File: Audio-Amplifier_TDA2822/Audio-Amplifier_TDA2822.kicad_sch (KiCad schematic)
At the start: 33 parts, among them J1 Conn_SPKR_L, J2 Conn_SPKR_L, U1 TDA2822M_2, U2 NE5532

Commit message: class D amp
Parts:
- C11, C12, C13, C7, C8, C9: footprint (none) -> Capacitor_THT:CP_Radial_D5.0mm_P2.50mm
- U1: footprint (none) -> Package_DIP:DIP-8_W7.62mm_LongPads
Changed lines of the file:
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@@
 			)
 		)
-		(property "Footprint" ""
+		(property "Footprint" "Package_DIP:DIP-8_W7.62mm_LongPads"
 			(at 167.64 43.18 0)
 			(effects
@@
 			)
 		)
-		(property "Footprint" ""
+		(property "Footprint" "Capacitor_THT:CP_Radial_D5.0mm_P2.50mm"
 			(at 172.72 59.3852 0)
 			(effects
@@
 			)
 		)
-		(property "Footprint" ""
+		(property "Footprint" "Capacitor_THT:CP_Radial_D5.0mm_P2.50mm"
 			(at 175.26 120.3452 0)
 			(effects
@@
 			)
 		)
-		(property "Footprint" ""
+		(property "Footprint" "Capacitor_THT:CP_Radial_D5.0mm_P2.50mm"
 			(at 31.4452 83.82 0)
 			(effects
@@
 			)
 		)
-		(property "Footprint" ""
+		(property "Footprint" "Capacitor_THT:CP_Radial_D5.0mm_P2.50mm"
 			(at 129.2352 165.1 0)
 			(effects
@@
 			)
 		)
-		(property "Footprint" ""
+		(property "Footprint" "Package_DIP:DIP-8_W7.62mm_LongPads"
 			(at 60.96 92.71 0)
 			(effects
@@
 			)
 		)
-		(property "Footprint" ""
+		(property "Footprint" "Capacitor_THT:CP_Radial_D5.0mm_P2.50mm"
 			(at 190.1952 62.23 0)
 			(effects
@@
 			)
 		)
-		(property "Footprint" ""
+		(property "Footprint" "Capacitor_THT:CP_Radial_D5.0mm_P2.50mm"
 			(at 186.69 103.1748 0)
 			(effects
@@
 			)
 		)
-		(property "Footprint" ""
+		(property "Footprint" "Package_DIP:DIP-8_W7.62mm_LongPads"
 			(at 167.64 104.14 0)
 			(effects

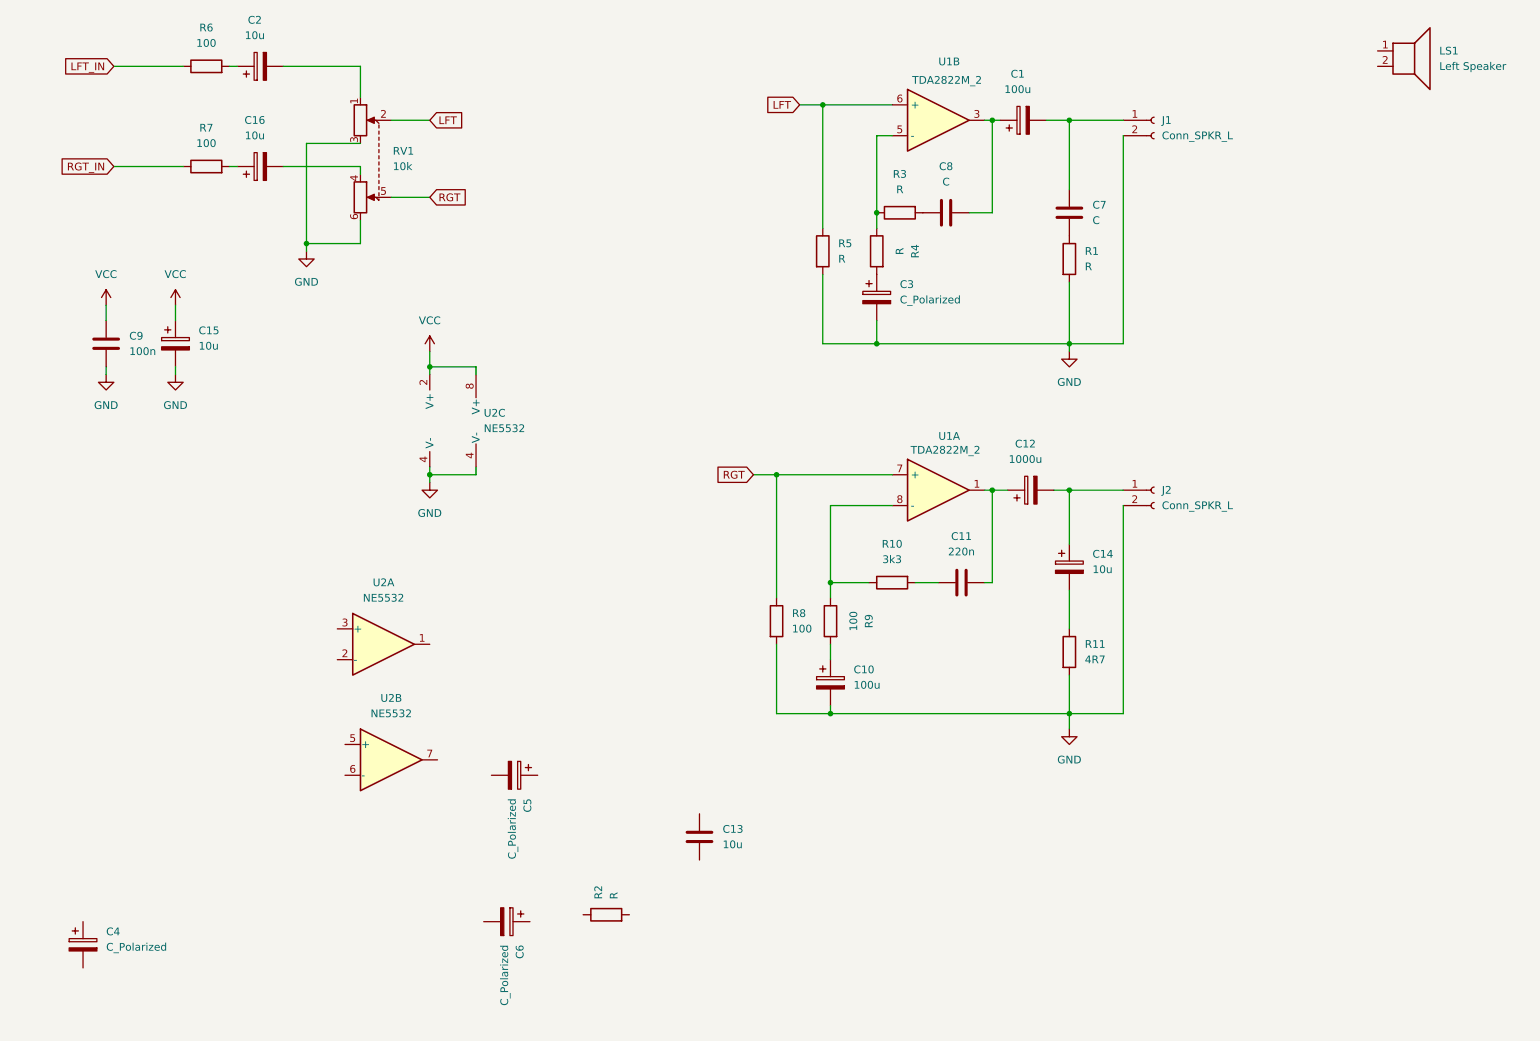
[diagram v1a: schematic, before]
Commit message: class D amp
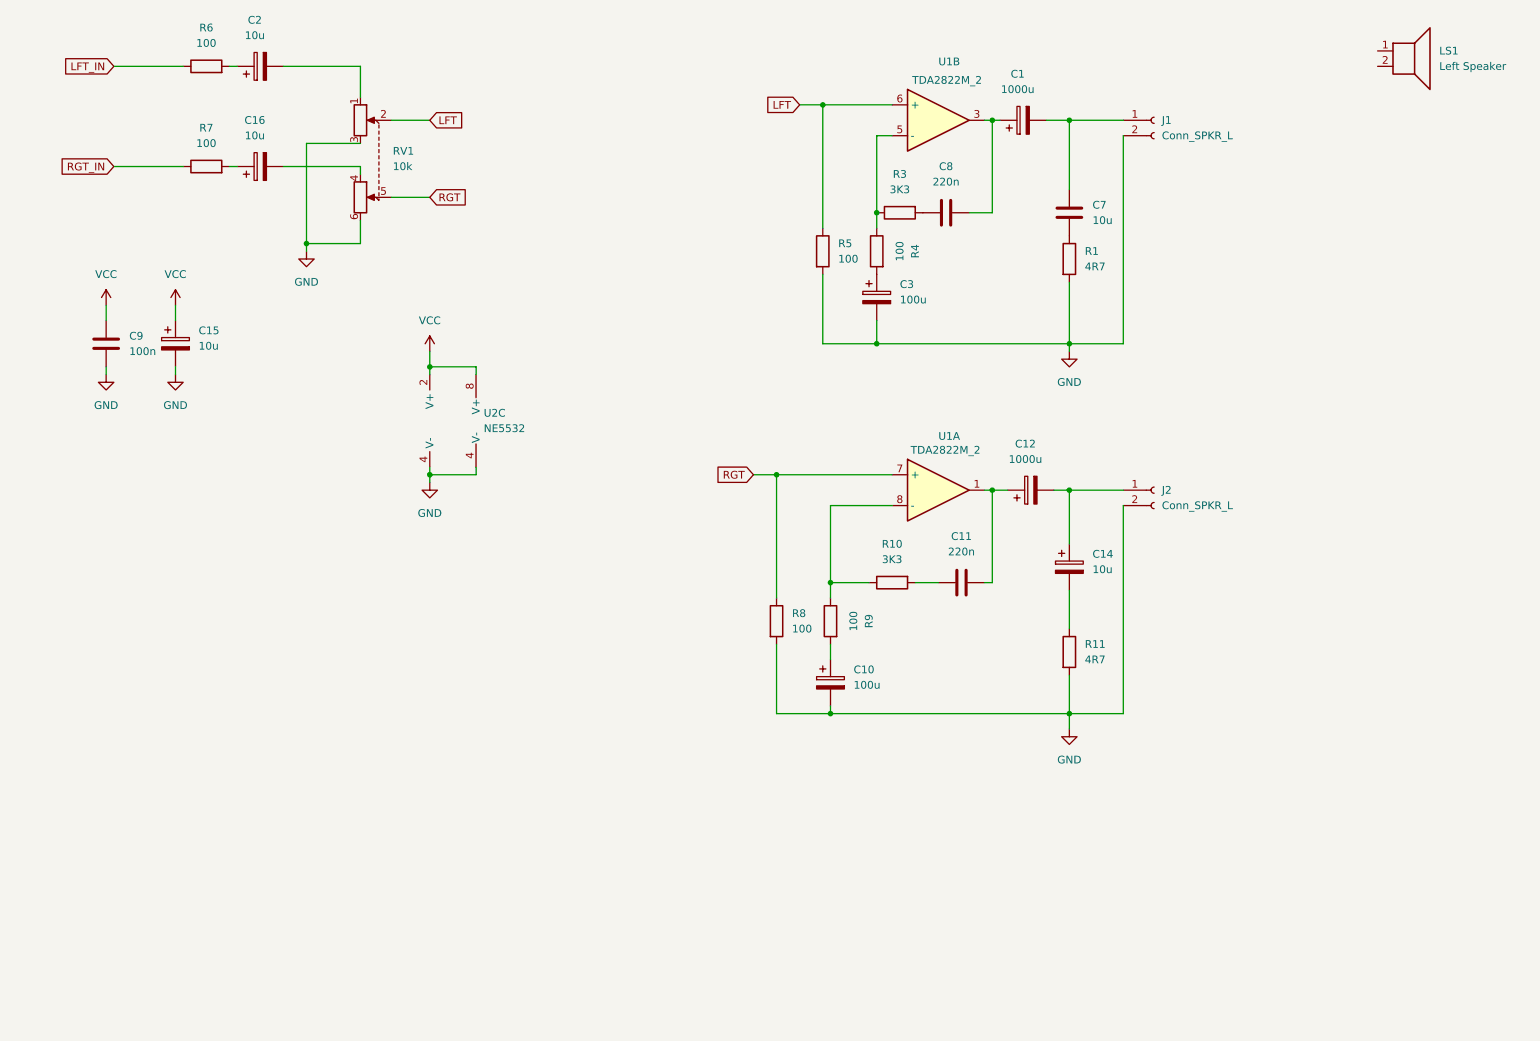
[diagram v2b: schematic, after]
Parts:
- removed C13: 10u, Capacitor_THT:CP_Radial_D5.0mm_P2.50mm, symbol Device:C
- removed C4, C5, C6: C_Polarized, Capacitor_THT:CP_Radial_D5.0mm_P2.50mm, symbol Device:C_Polarized
- removed R2: R, Resistor_THT:R_Axial_DIN0204_L3.6mm_D1.6mm_P5.08mm_Vertical, symbol Device:R
- removed unit 1 of U2
- removed unit 2 of U2
- C1: value 100u -> 1000u
- C3: value C_Polarized -> 100u
- C7: value C -> 10u
- C8: value C -> 220n
- R1: value R -> 4R7
- R10: value 3k3 -> 3K3
- R3: value R -> 3K3
- R4, R5: value R -> 100
- RV1: footprint Potentiometer_SMD:Potentiometer_Bourns_3224G_Horizontal -> Potentiometer_THT:Potentiometer_Bourns_PTV112-4_Dual_Vertical

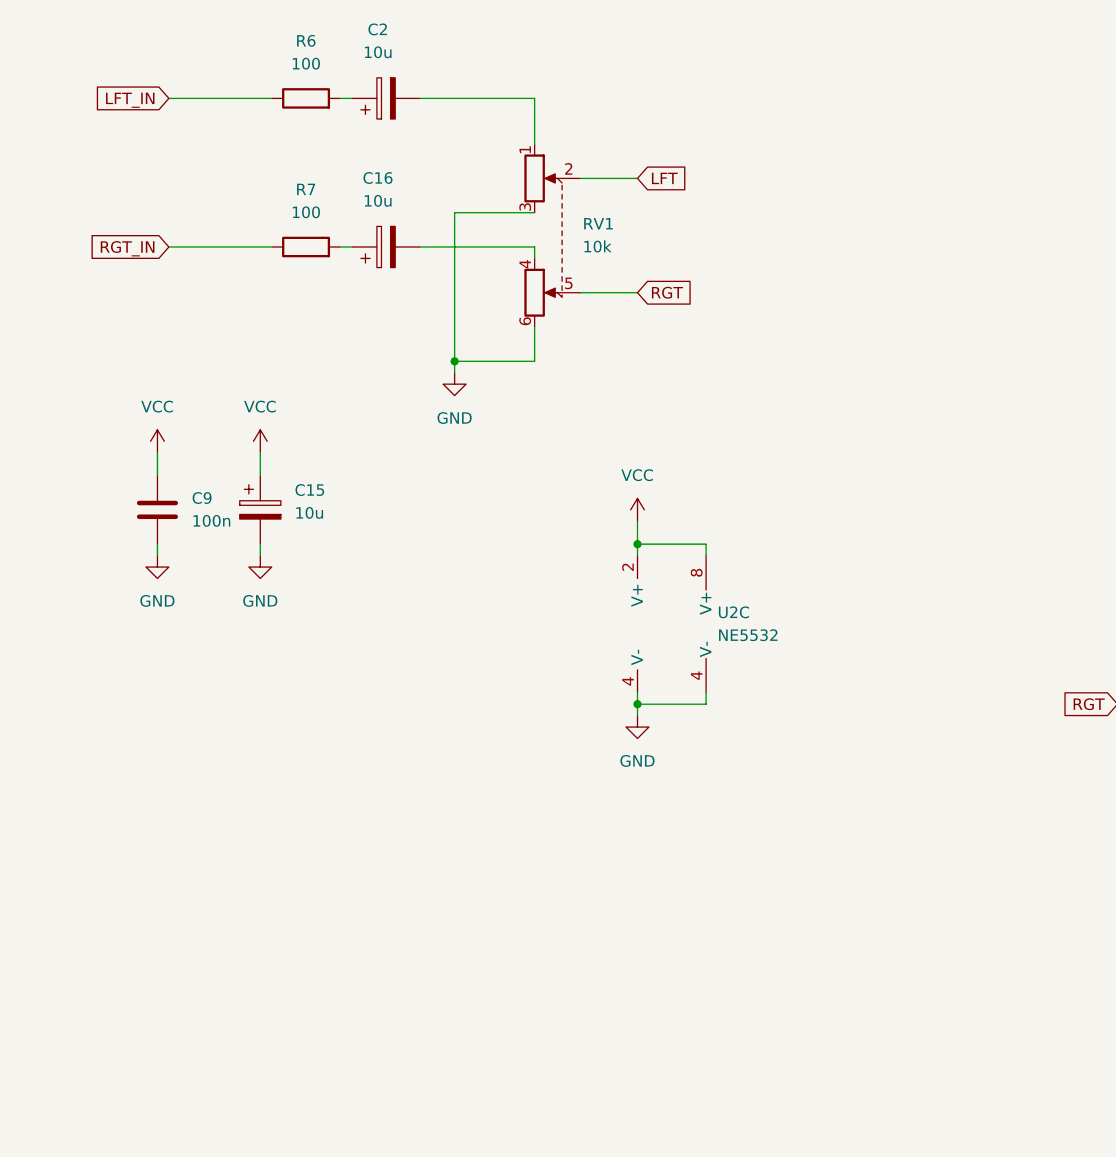
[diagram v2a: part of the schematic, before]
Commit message: class D amp
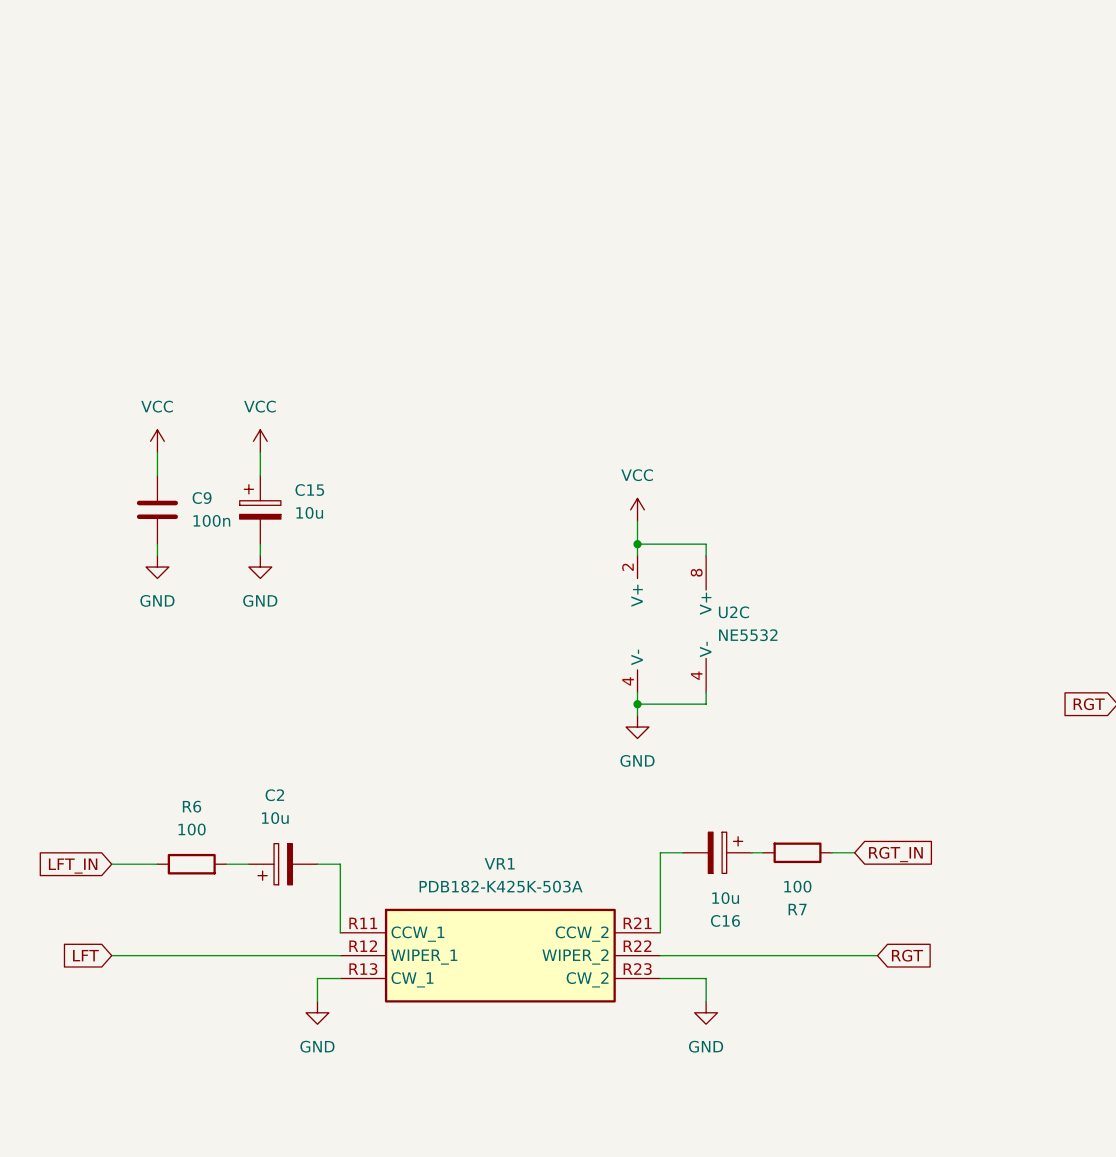
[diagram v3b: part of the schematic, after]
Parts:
- removed RV1: 10k, Potentiometer_THT:Potentiometer_Bourns_PTV112-4_Dual_Vertical, symbol Device:R_Potentiometer_Dual
- added VR1: PDB182-K425K-503A, PDB182K425K503A, symbol project:PDB182-K425K-503A
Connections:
- net GND: now also VR1.R13 (CW_1), VR1.R23 (CW_2)
- net LFT: now also VR1.R12 (WIPER_1)
- net RGT: now also VR1.R22 (WIPER_2)
- net at C16.2: now also VR1.R21 (CCW_2)
- net at C2.2: now also VR1.R11 (CCW_1)
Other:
- moved on the sheet: C16, C2, R6, R7

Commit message: class D amp
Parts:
- C1, U2: footprint (none) -> Capacitor_THT:CP_Radial_D8.0mm_P5.00mm
- C12: footprint Capacitor_THT:CP_Radial_D5.0mm_P2.50mm -> Capacitor_THT:CP_Radial_D8.0mm_P5.00mm
- VR1: footprint PDB182K425K503A -> project:PDB182K425K503A
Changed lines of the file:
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@@
 			)
 		)
-		(property "Footprint" ""
+		(property "Footprint" "Capacitor_THT:CP_Radial_D8.0mm_P5.00mm"
 			(at 185.42 42.2148 0)
 			(effects
@@
 			)
 		)
-		(property "Footprint" "PDB182K425K503A"
+		(property "Footprint" "project:PDB182K425K503A"
 			(at 82.55 221.92 0)
 			(effects
@@
 			)
 		)
-		(property "Footprint" "Capacitor_THT:CP_Radial_D5.0mm_P2.50mm"
+		(property "Footprint" "Capacitor_THT:CP_Radial_D8.0mm_P5.00mm"
 			(at 186.69 103.1748 0)
 			(effects
@@
 			)
 		)
-		(property "Footprint" ""
+		(property "Footprint" "Capacitor_THT:CP_Radial_D8.0mm_P5.00mm"
 			(at 93.98 92.71 0)
 			(effects

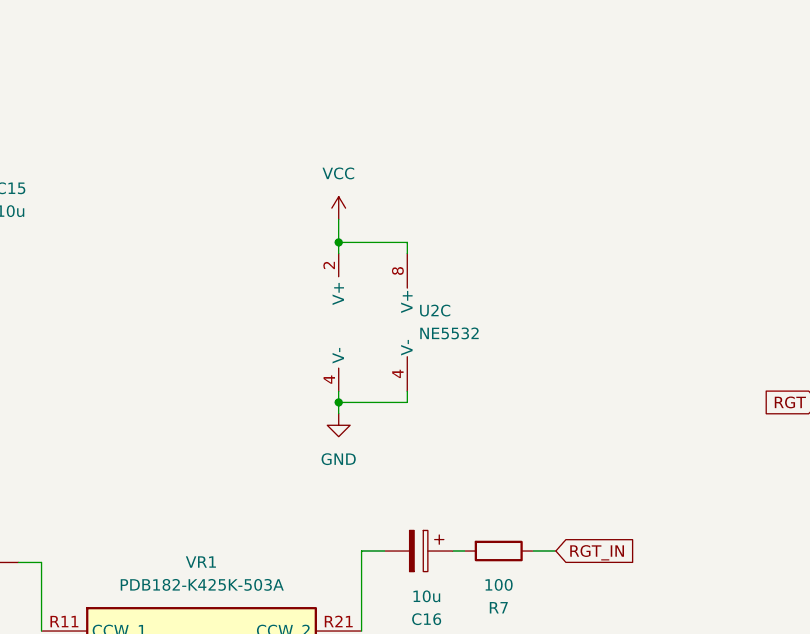
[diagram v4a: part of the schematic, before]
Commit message: class D amp
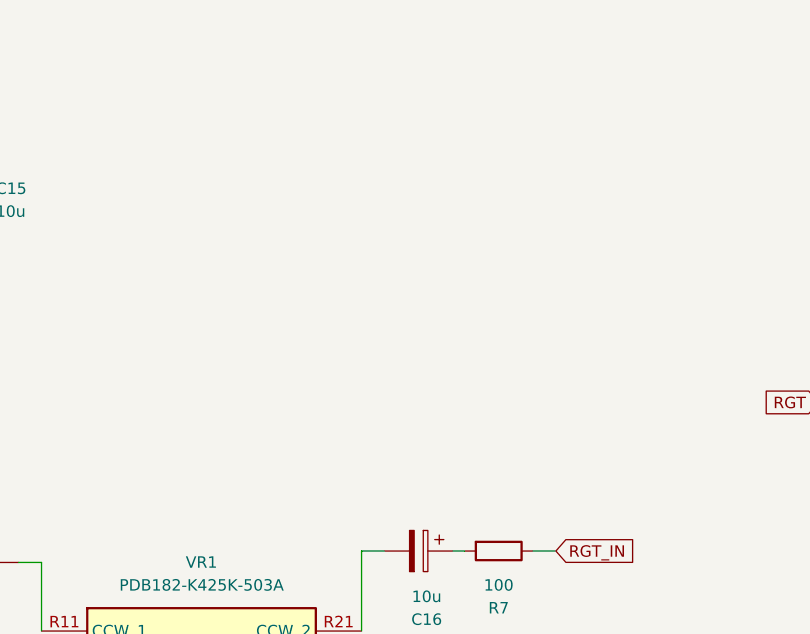
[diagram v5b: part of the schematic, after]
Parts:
- removed unit 3 of U1
- removed U2: NE5532, Capacitor_THT:CP_Radial_D8.0mm_P5.00mm, symbol Amplifier_Operational:NE5532

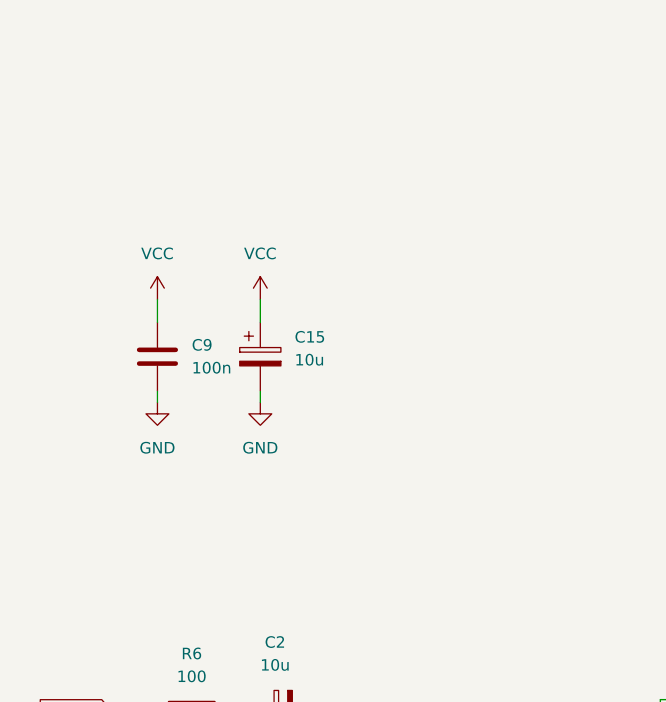
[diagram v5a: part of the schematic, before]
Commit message: class D amp
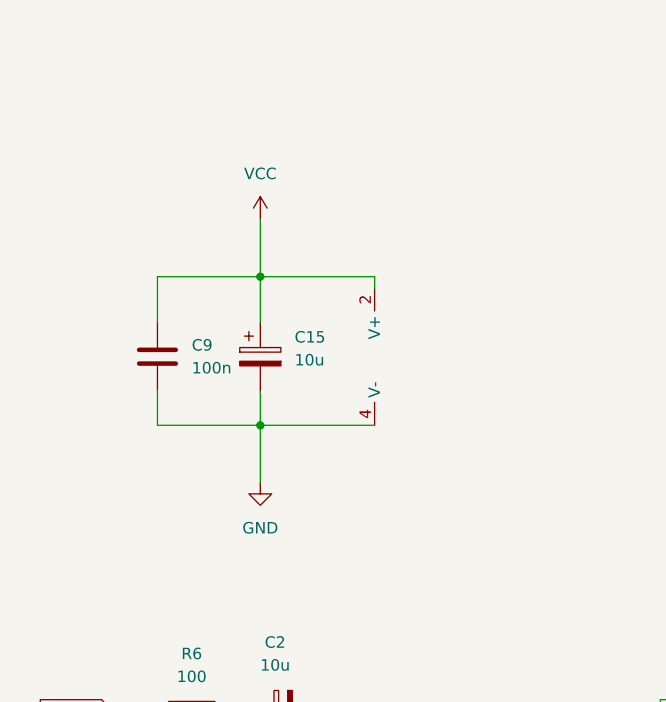
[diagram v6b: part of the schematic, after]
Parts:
- added unit 3 of U1
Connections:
- net GND: now also U1.4 (V-)
- net VCC: now also U1.2 (V+)

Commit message: class D amp
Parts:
- C15, C9: footprint Capacitor_THT:CP_Radial_D5.0mm_P2.50mm -> Capacitor_THT:C_Disc_D5.0mm_W2.5mm_P2.50mm
- U1: footprint (none) -> Package_DIP:DIP-8_W7.62mm_LongPads
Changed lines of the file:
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@@
 			)
 		)
-		(property "Footprint" ""
+		(property "Footprint" "Package_DIP:DIP-8_W7.62mm_LongPads"
 			(at 31.75 80.01 0)
 			(effects
@@
 			)
 		)
-		(property "Footprint" "Capacitor_THT:CP_Radial_D5.0mm_P2.50mm"
+		(property "Footprint" "Capacitor_THT:C_Disc_D5.0mm_W2.5mm_P2.50mm"
 			(at 42.8752 83.82 0)
 			(effects
@@
 			)
 		)
-		(property "Footprint" "Capacitor_THT:CP_Radial_D5.0mm_P2.50mm"
+		(property "Footprint" "Capacitor_THT:C_Disc_D5.0mm_W2.5mm_P2.50mm"
 			(at 31.4452 83.82 0)
 			(effects

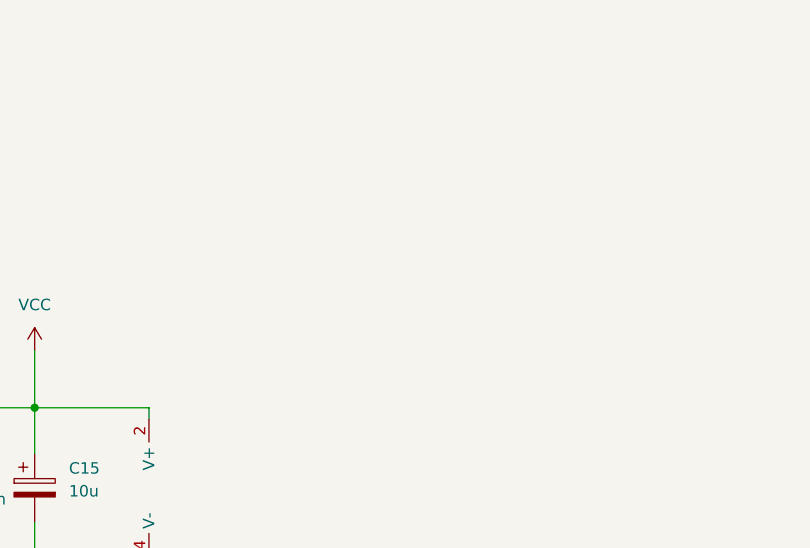
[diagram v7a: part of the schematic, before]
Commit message: class D amp
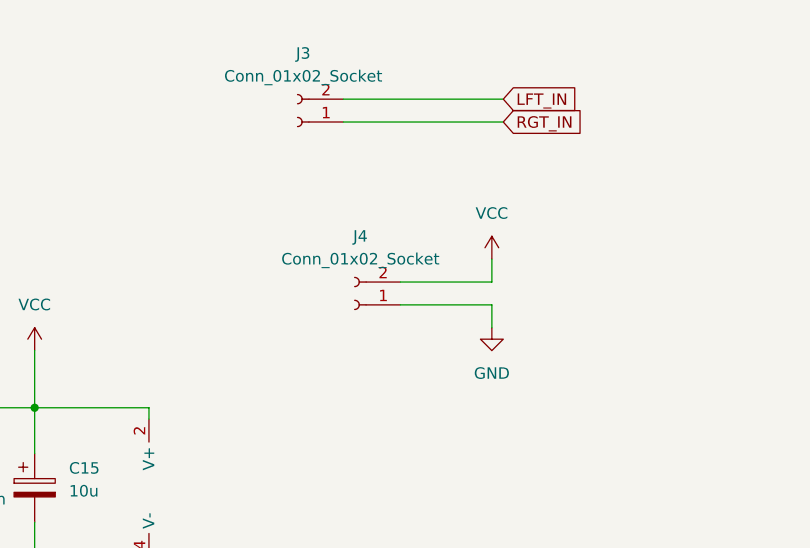
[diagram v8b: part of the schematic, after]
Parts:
- added J3, J4: Conn_01x02_Socket, Connector_PinHeader_2.54mm:PinHeader_1x02_P2.54mm_Vertical, symbol Connector:Conn_01x02_Socket
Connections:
- net GND: now also J4.1 (Pin_1)
- net LFT_IN: now also J3.2 (Pin_2)
- net RGT_IN: now also J3.1 (Pin_1)
- net VCC: now also J4.2 (Pin_2)
